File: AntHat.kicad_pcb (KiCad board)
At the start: 4 copper layers, 65 x 56.5 mm, 5 parts, among them J1 Raspberry_Pi_2_3

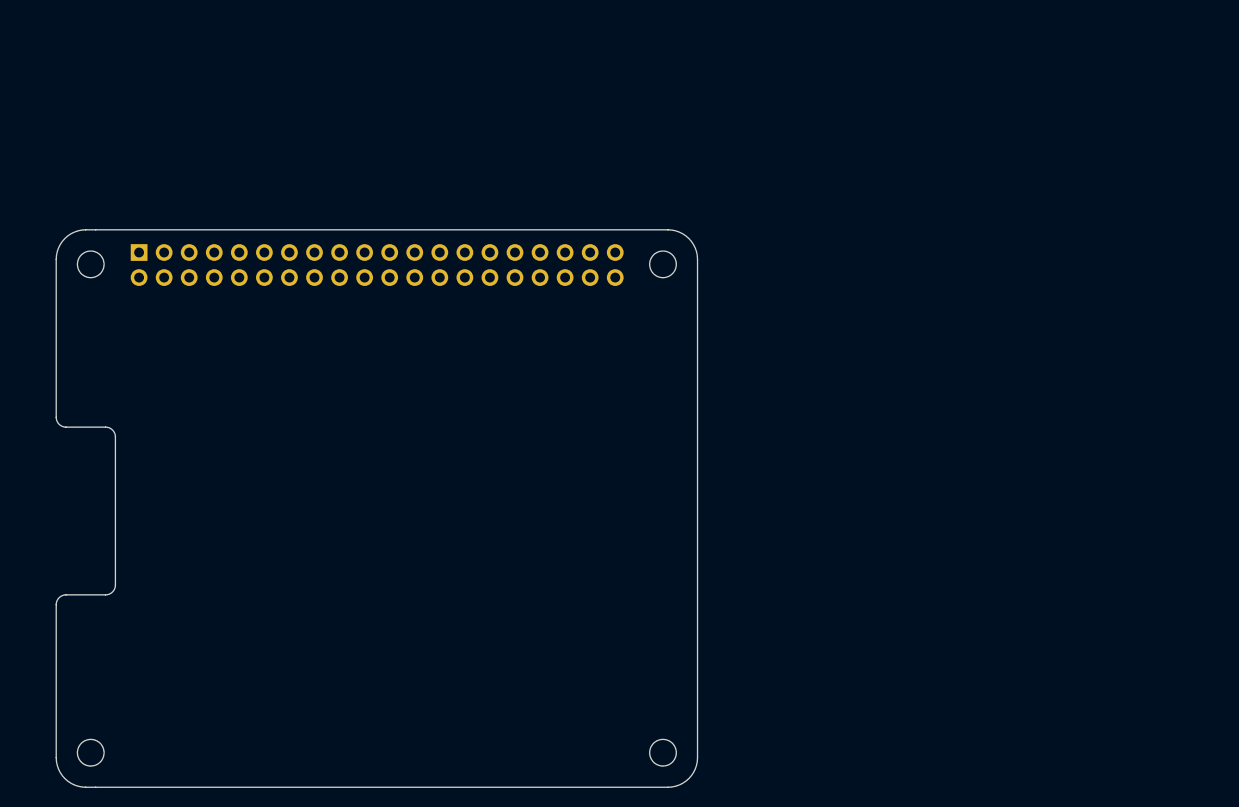
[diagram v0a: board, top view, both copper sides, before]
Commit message: finished routing. added logo
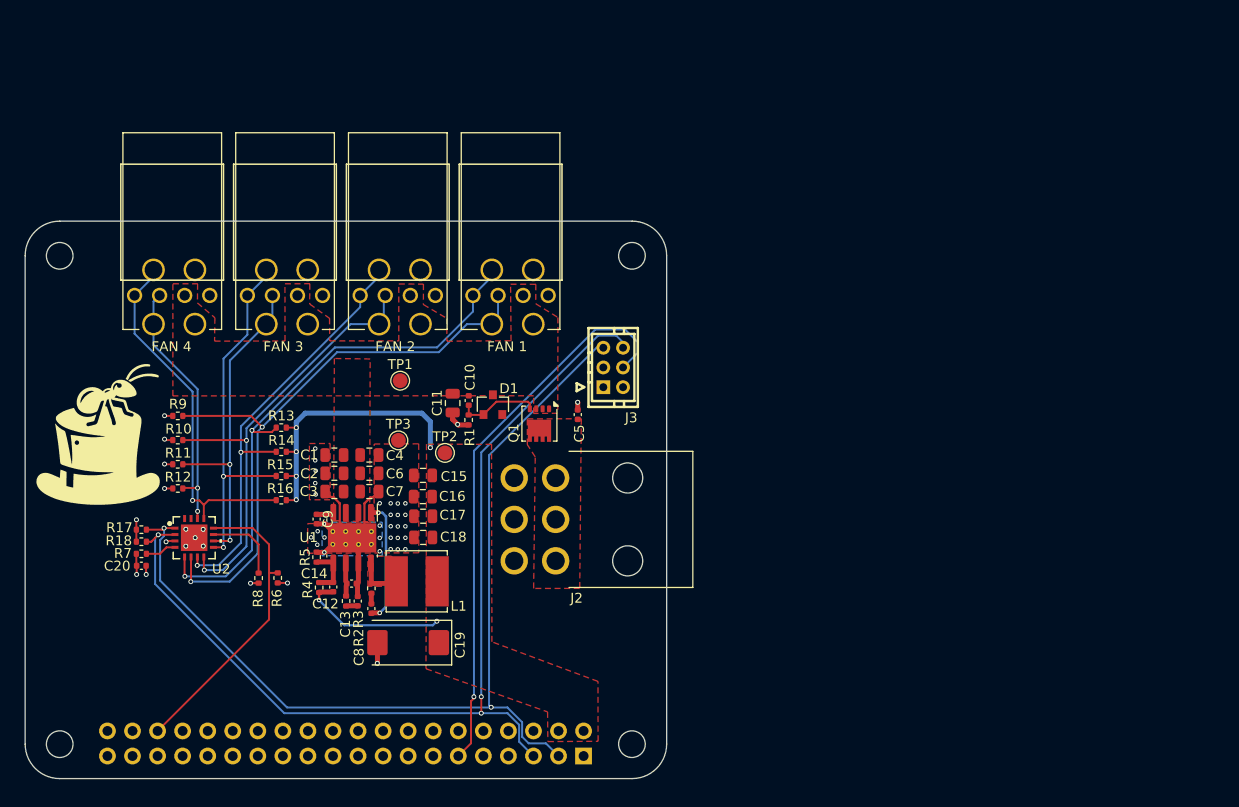
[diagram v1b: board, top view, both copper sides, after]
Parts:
- added C1: 10uF 35v, Capacitor_SMD:C_0805_2012Metric, F.Cu at (138.5, 93.0)
- added C10: 0.1uF, Capacitor_SMD:C_0402_1005Metric, F.Cu at (152.1, 87.5)
- added C11: 10u 35v, Capacitor_SMD:C_0805_2012Metric, F.Cu at (150.5, 87.7)
- added C12: nf, Capacitor_SMD:C_0402_1005Metric, F.Cu at (140.2, 106.0)
- added C13: 1.2nF, Capacitor_SMD:C_0402_1005Metric, F.Cu at (140.8, 107.8)
- added C14: nf, Capacitor_SMD:C_0402_1005Metric, F.Cu at (138.4, 106.4)
- added C15: 10uF, Capacitor_SMD:C_0805_2012Metric, F.Cu at (147.5, 95.1)
- added C16: 10uF, Capacitor_SMD:C_0805_2012Metric, F.Cu at (147.4, 97.2)
- added C17: 10uF, Capacitor_SMD:C_0805_2012Metric, F.Cu at (147.5, 99.2)
- added C18: 10uF, Capacitor_SMD:C_0805_2012Metric, F.Cu at (147.5, 101.4)
- added C19: 100uF, Capacitor_Tantalum_SMD:CP_EIA-7343-31_Kemet-D, F.Cu at (146.0, 112.0)
- added C2: 10uF 35v, Capacitor_SMD:C_0805_2012Metric, F.Cu at (138.5, 94.9)
- added C20: 0.1uF, Capacitor_SMD:C_0402_1005Metric, F.Cu at (118.9, 104.2)
- added C3: 10uF 35v, Capacitor_SMD:C_0805_2012Metric, F.Cu at (138.5, 96.7)
- added C4: 10uF 35v, Capacitor_SMD:C_0805_2012Metric, F.Cu at (142.0, 93.0)
- added C5: 100n 100v, Capacitor_SMD:C_0402_1005Metric, F.Cu at (163.2, 88.9)
- added C6: 10uF 35v, Capacitor_SMD:C_0805_2012Metric, F.Cu at (142.0, 94.9)
- added C7: 10uF 35v, Capacitor_SMD:C_0805_2012Metric, F.Cu at (142.0, 96.7)
- added C8: 0.1uF, Capacitor_SMD:C_0402_1005Metric, F.Cu at (142.2, 108.6)
- added C9: 0.1uF, Capacitor_SMD:C_0402_1005Metric, F.Cu at (136.7, 99.5)
- added D1: MMBZ5242BLT3G, AntHat:D_SOT-23_ANK, F.Cu at (154.6, 87.9)
- added G***: LOGO, AntHat:logo, F.Cu at (114.4, 91.6)
- added J10: 0353180420, AntHat:MOLEX_353180420, F.Cu at (131.6, 74.2)
- added J11: 0353180420, AntHat:MOLEX_353180420, F.Cu at (120.2, 74.2)
- added J2: 0455580003, AntHat:0455580003, F.Cu at (160.9, 95.3)
- added J3: PSU Comm, AntHat:CONN-TH_6P-P2.00_PHD-2X3A, F.Cu at (166.7, 84.1)
- added J4: 61900411021, AntHat:CONN_61900411021_WRE, F.Cu at (160.2, 76.8)
- added J5: 61900411021, AntHat:CONN_61900411021_WRE, F.Cu at (148.7, 76.8)
- added J6: 61900411021, AntHat:CONN_61900411021_WRE, F.Cu at (137.3, 76.8)
- added J7: 61900411021, AntHat:CONN_61900411021_WRE, F.Cu at (125.8, 76.8)
- added J8: 0353180420, AntHat:MOLEX_353180420, F.Cu at (154.4, 74.2)
- added J9: 0353180420, AntHat:MOLEX_353180420, F.Cu at (143.0, 74.2)
- added L1: SRN6045TA-3R3Y, Inductor_SMD:L_Bourns_SRN6045TA, F.Cu at (146.8, 105.8)
- added Q1: DMP3013SFV-7, Package_SON:Diodes_PowerDI3333-8, F.Cu at (159.3, 89.8)
- added R1: 12k 1%, Resistor_SMD:R_0402_1005Metric, F.Cu at (152.1, 89.5)
- added R10: 36K, Resistor_SMD:R_0402_1005Metric, F.Cu at (122.6, 91.5)
- added R11: 36K, Resistor_SMD:R_0402_1005Metric, F.Cu at (122.6, 93.9)
- added R12: 36K, Resistor_SMD:R_0402_1005Metric, F.Cu at (122.6, 96.4)
- added R13: 10k, Resistor_SMD:R_0402_1005Metric, F.Cu at (133.1, 90.2)
- added R14: 10k, Resistor_SMD:R_0402_1005Metric, F.Cu at (133.1, 92.7)
- added R15: 10k, Resistor_SMD:R_0402_1005Metric, F.Cu at (133.1, 95.1)
- added R16: 10k, Resistor_SMD:R_0402_1005Metric, F.Cu at (133.1, 97.6)
- added R17: 4.7k, Resistor_SMD:R_0402_1005Metric, F.Cu at (118.9, 100.6)
- added R18: 4.7k, Resistor_SMD:R_0402_1005Metric, F.Cu at (118.9, 101.8)
- added R2: 10, Resistor_SMD:R_0402_1005Metric, F.Cu at (142.2, 106.5)
- added R3: 20k, Resistor_SMD:R_0402_1005Metric, F.Cu at (139.7, 107.8)
- added R4: 12k, Resistor_SMD:R_0402_1005Metric, F.Cu at (136.9, 106.4)
- added R5: 2.2k, Resistor_SMD:R_0402_1005Metric, F.Cu at (136.7, 103.4)
- added R6: 4.7k, Resistor_SMD:R_0402_1005Metric, F.Cu at (132.7, 105.5)
- added R7: 33k, Resistor_SMD:R_0402_1005Metric, F.Cu at (118.9, 103.0)
- added R8: 22k, Resistor_SMD:R_0402_1005Metric, F.Cu at (130.8, 105.5)
- added R9: 36K, Resistor_SMD:R_0402_1005Metric, F.Cu at (122.6, 89.0)
- added TP1: TestPoint, TestPoint:TestPoint_Pad_D1.5mm, F.Cu at (145.2, 85.5)
- added TP2: TestPoint, TestPoint:TestPoint_Pad_D1.5mm, F.Cu at (149.7, 92.8)
- added TP3: TestPoint, TestPoint:TestPoint_Pad_D1.5mm, F.Cu at (145.0, 91.5)
- added U1: AP64501SP-13, Package_SO:SOIC-8-1EP_3.9x4.9mm_P1.27mm_EP2.95x4.9mm_Mask2.71x3.4mm_ThermalVias, F.Cu at (140.3, 101.4)
- added U2: EMC2305, AntHat:QFN16_4x4MC_MCH, F.Cu at (124.3, 101.4)
- J1: footprint pihat:ESQ-120-14-T-D -> AntHat:ESQ-120-14-T-D
- moved H4 79.2 mm to (110.6, 72.8), turned to -90 degrees
- moved H2 78.1 mm to (110.6, 122.3), turned to -90 degrees
- moved H3 74.5 mm to (168.6, 72.8), turned to -90 degrees
- moved H1 73.3 mm to (168.6, 122.3), turned to -90 degrees
- moved J1 68.1 mm to (163.7, 123.5), turned to 90 degrees
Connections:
- J1 pad 1: unconnected-(J1-3V3-Pad1) -> /+3.3v
- J1 pad 11: unconnected-(J1-GPIO17-Pad11) -> /PSU_EN
- J1 pad 14: unconnected-(J1-GND-Pad14) -> GND
- J1 pad 17: unconnected-(J1-3V3-Pad17) -> /+3.3v
- J1 pad 2: unconnected-(J1-5V-Pad2) -> /5V
- J1 pad 20: unconnected-(J1-GND-Pad20) -> GND
- J1 pad 25: unconnected-(J1-GND-Pad25) -> GND
- J1 pad 3: unconnected-(J1-SDA/GPIO2-Pad3) -> /SDA
- J1 pad 30: unconnected-(J1-GND-Pad30) -> GND
- J1 pad 34: unconnected-(J1-GND-Pad34) -> GND
- J1 pad 36: unconnected-(J1-GPIO16-Pad36) -> /FAN_ALERT
- J1 pad 39: unconnected-(J1-GND-Pad39) -> GND
- J1 pad 4: unconnected-(J1-5V-Pad4) -> /5V
- J1 pad 5: unconnected-(J1-SCL/GPIO3-Pad5) -> /SCL
- J1 pad 6: unconnected-(J1-GND-Pad6) -> GND
- J1 pad 9: unconnected-(J1-GND-Pad9) -> GND
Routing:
- net /SCL: track 0.00 -> 101.4 mm, vias 0 -> 3
- net /SDA: track 0.00 -> 98.8 mm, vias 0 -> 2
- net /TACH1: track 0.00 -> 62.8 mm, vias 0 -> 2
- net /PWM1: track 0.00 -> 57.1 mm, vias 0 -> 2
- net /PSU_EN: track 0.00 -> 57.0 mm, vias 0 -> 1
- net /TACH2: track 0.00 -> 46.0 mm, vias 0 -> 2
- net /5V: track 0.00 -> 44.1 mm, vias 0 -> 7
- net /PWM2: track 0.00 -> 43.3 mm, vias 0 -> 2
- net /PWM4: track 0.00 -> 36.9 mm, vias 0 -> 1
- net /PWM3: track 0.00 -> 36.3 mm, vias 0 -> 2
- net /TACH3: track 0.00 -> 33.1 mm, vias 0 -> 2
- net /FAN_ALERT: track 0.00 -> 30.8 mm
- net /TACH4: track 0.00 -> 26.2 mm, vias 0 -> 2
- net GND: track 0.00 -> 23.6 mm, vias 0 -> 39
- net Net-(U1-BST): track 0.00 -> 12.5 mm, vias 0 -> 2
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- added copper zone on In2.Cu, net /+3.3v
- added copper zone on F.Cu, net /12V
- added copper zone on F.Cu, net /5V
- added copper zone on F.Cu, net /VIN
- added copper zone on B.Cu, net GND
- added copper zone on F.Cu, net GND
- added copper zone on In1.Cu, net GND
- added copper zone on F.Cu, net Net-(U1-SW)
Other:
- outline, holes or cut-outs redrawn
- board text added: "FAN 1"
- board text added: "FAN 2"
- board text added: "FAN 3"
- board text added: "FAN 4"

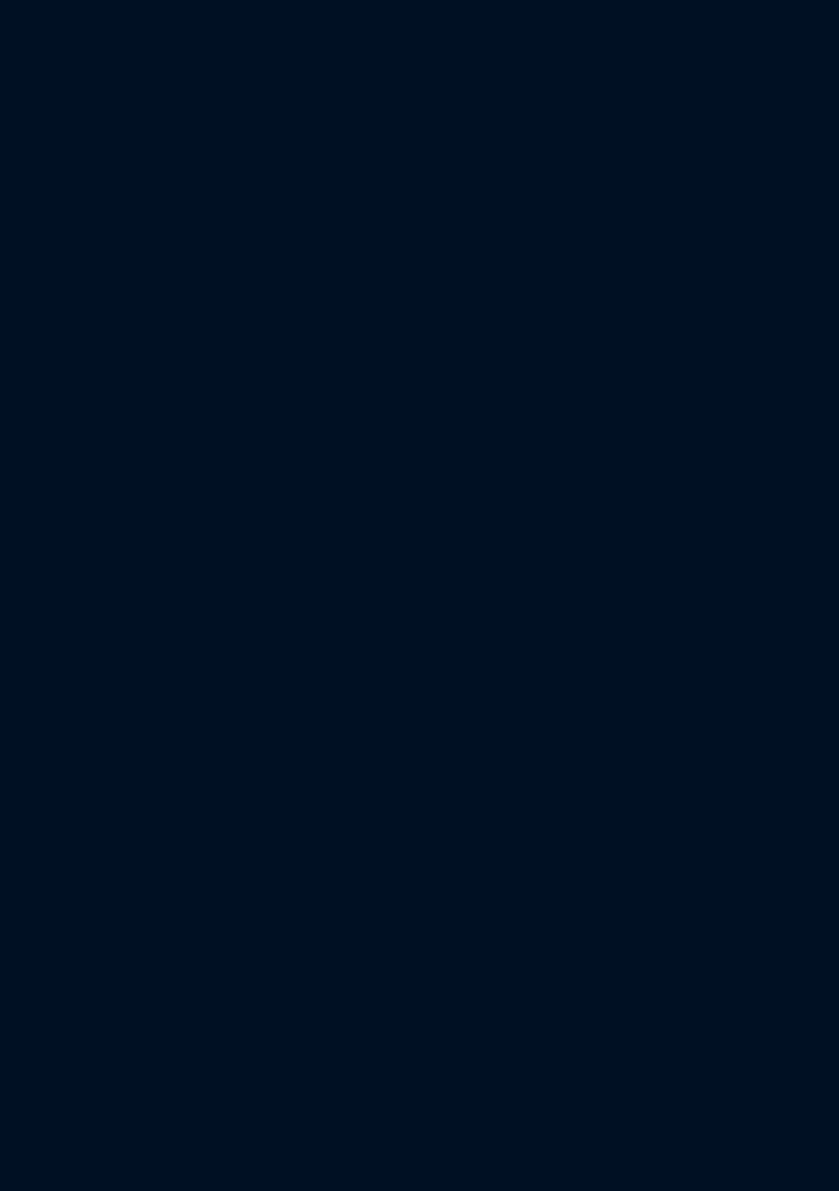
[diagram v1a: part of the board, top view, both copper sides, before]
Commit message: added the TPS54531 since the AP64501SP-13 isn't on DK. prolly will delete
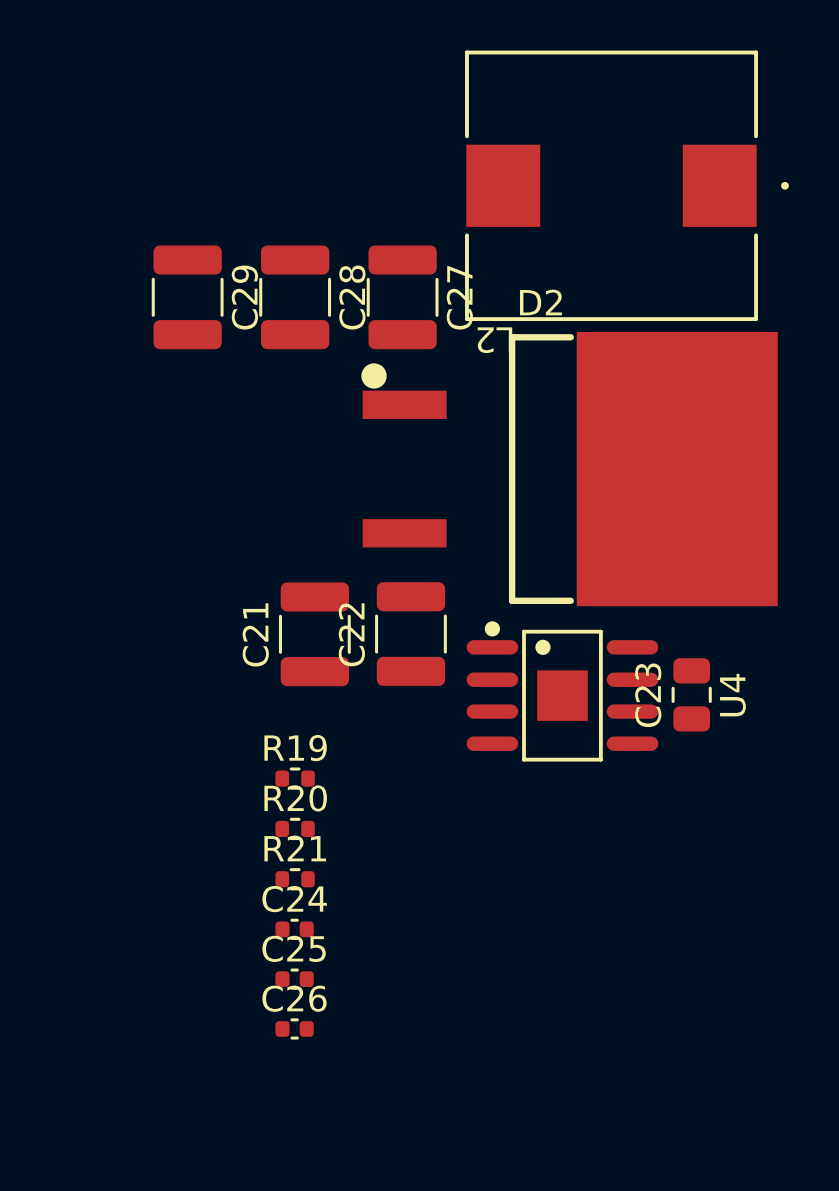
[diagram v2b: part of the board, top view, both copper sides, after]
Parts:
- added C21: 10uF, Capacitor_SMD:C_1210_3225Metric, F.Cu at (209.4, 78.5)
- added C22: 10uF, Capacitor_SMD:C_1210_3225Metric, F.Cu at (213.2, 78.5)
- added C23: 10pF, Capacitor_SMD:C_0805_2012Metric, F.Cu at (224.3, 80.9)
- added C24: 1.1nF, Capacitor_SMD:C_0402_1005Metric, F.Cu at (208.6, 90.2)
- added C25: 8.2nF, Capacitor_SMD:C_0402_1005Metric, F.Cu at (208.6, 92.2)
- added C26: 0.1uF, Capacitor_SMD:C_0402_1005Metric, F.Cu at (208.6, 94.2)
- added C27: 47uF, Capacitor_SMD:C_1210_3225Metric, F.Cu at (212.9, 65.2)
- added C28: 47uF, Capacitor_SMD:C_1210_3225Metric, F.Cu at (208.6, 65.2)
- added C29: 47uF, Capacitor_SMD:C_1210_3225Metric, F.Cu at (204.4, 65.2)
- added D2: STPS20M100SG-TR, AntHat:D2PAK_L10.4-W8.5-P2.54-LS15.4-BR, F.Cu at (218.3, 72.0)
- added L2: 6.8uH, AntHat:IND_IHLP-4040DZ_VIS, F.Cu at (221.1, 60.8)
- added R19: 31.6k, Resistor_SMD:R_0402_1005Metric, F.Cu at (208.6, 84.2)
- added R20: 10.2k, Resistor_SMD:R_0402_1005Metric, F.Cu at (208.6, 86.2)
- added R21: 1.96k, Resistor_SMD:R_0402_1005Metric, F.Cu at (208.6, 88.2)
- added U4: TPS54531DDAR, AntHat:SOIC-8_L5.0-W4.0-P1.27-LS6.0-BL-EP2.0, F.Cu at (219.2, 81.0)
- C11: value 10u 35v -> 10uF 35v
- C12, C14: value nf -> ~
- C5: value 100n 100v -> 0.1uF 100v
- L1: value SRN6045TA-3R3Y -> 3.3uH

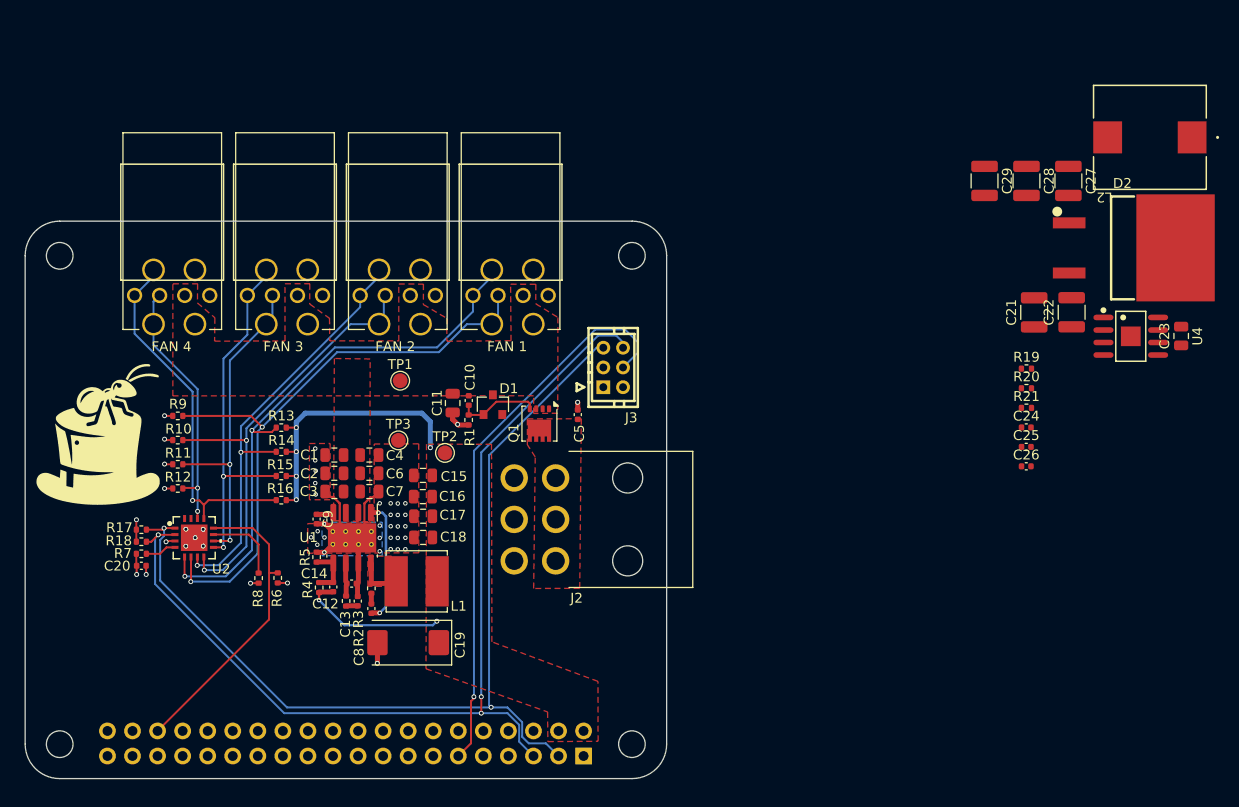
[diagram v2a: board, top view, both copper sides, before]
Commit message: deleted TPS54531. Changed OOS Inductor. DRC passes
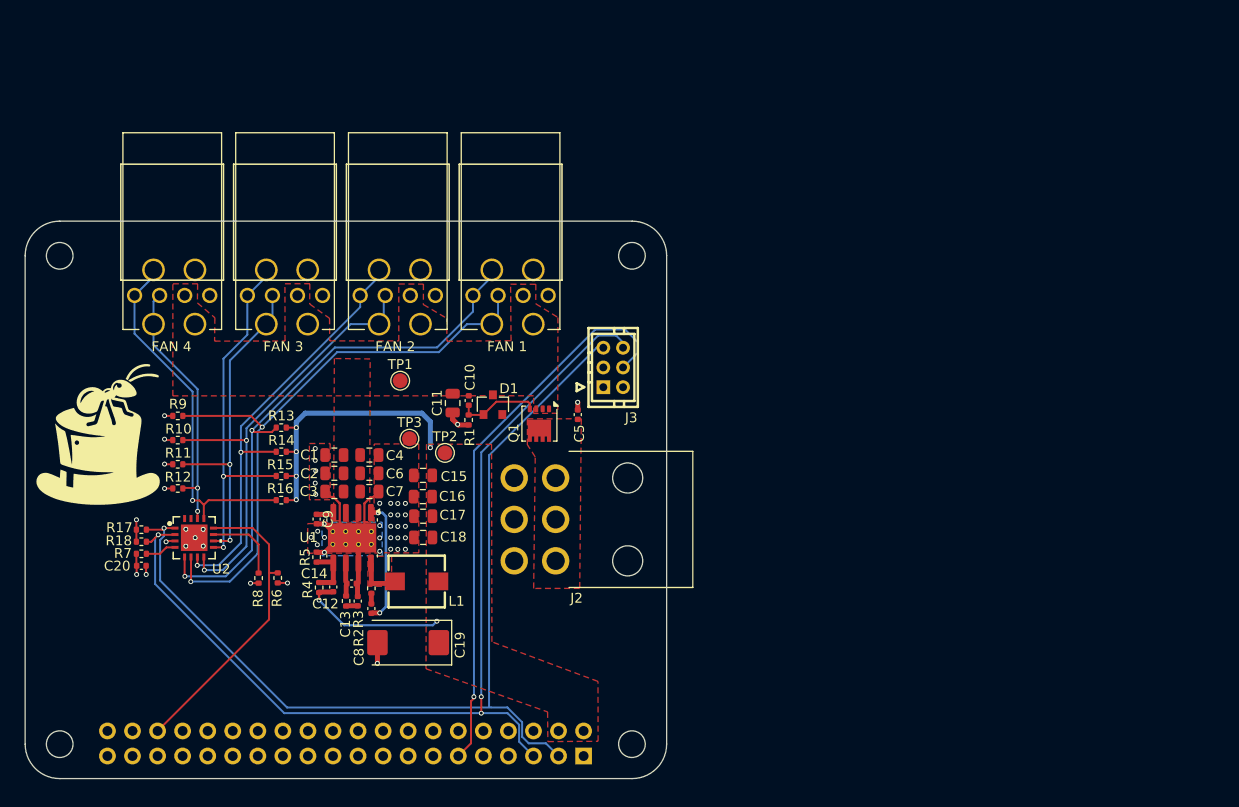
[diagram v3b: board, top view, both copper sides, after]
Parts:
- removed C21, C22: 10uF, Capacitor_SMD:C_1210_3225Metric
- removed C23: 10pF, Capacitor_SMD:C_0805_2012Metric
- removed C24: 1.1nF, Capacitor_SMD:C_0402_1005Metric
- removed C25: 8.2nF, Capacitor_SMD:C_0402_1005Metric
- removed C26: 0.1uF, Capacitor_SMD:C_0402_1005Metric
- removed C27, C28, C29: 47uF, Capacitor_SMD:C_1210_3225Metric
- removed D2: STPS20M100SG-TR, AntHat:D2PAK_L10.4-W8.5-P2.54-LS15.4-BR
- removed L2: 6.8uH, AntHat:IND_IHLP-4040DZ_VIS
- removed R19: 31.6k, Resistor_SMD:R_0402_1005Metric
- removed R20: 10.2k, Resistor_SMD:R_0402_1005Metric
- removed R21: 1.96k, Resistor_SMD:R_0402_1005Metric
- removed U4: TPS54531DDAR, AntHat:SOIC-8_L5.0-W4.0-P1.27-LS6.0-BL-EP2.0
- L1: footprint Inductor_SMD:L_Bourns_SRN6045TA -> AntHat:IND-SMD_L5.7-W5.2
- moved TP3 1.13 mm to (146.1, 91.3)
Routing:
- net /SDA: track 98.8 -> 98.7 mm, vias 2 -> 1

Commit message: DRC, ERC and added gerbers
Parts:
- C1, C11, C2, C3, C4, C6, C7: value 10uF 35v -> 10uF
- C13: value 1.2nF -> 1200pF
- R1: value 12k 1% -> 12k
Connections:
- net /+3.3v renamed /3V3
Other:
- board text added: "AntHat v1"
